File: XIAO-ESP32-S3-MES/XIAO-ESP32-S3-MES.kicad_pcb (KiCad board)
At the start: 2 copper layers, 36 x 39 mm, 11 parts, among them SW1 Conn_01x02_Socket, U2 XIAO-ESP32-S3-SMD

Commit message: SS 配置途中
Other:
- board text added: "5V G A B"
- board text added: "D P G 5V"
- board text added: "L H G 5V"
- board text added: "XIAO ESP32-S3 MES v1.0"
- board text removed: "5V0 G A B"
- board text removed: "D P G 5V0"
- board text removed: "L H G 5V0"
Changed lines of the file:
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@@
 		)
 		(fp_text user "${REFERENCE}"
-			(at 3.75 2.7 90)
-			(layer "F.Fab")
+			(at 3.75 2.7 -90)
+			(layer "B.SilkS")
 			(effects
 				(font
@@
 					(thickness 0.15)
 				)
+				(justify mirror)
 			)
 		)
@@
 		)
 		(fp_text user "${REFERENCE}"
-			(at 1.25 2.7 0)
-			(layer "F.Fab")
+			(at 1.25 2.7 -0)
+			(layer "B.SilkS")
 			(effects
 				(font
@@
 					(thickness 0.15)
 				)
+				(justify mirror)
 			)
 		)
@@
 		)
 		(fp_text user "${REFERENCE}"
-			(at 3.75 2.7 0)
-			(layer "F.Fab")
+			(at 3.75 2.7 -0)
+			(layer "B.SilkS")
 			(effects
 				(font
@@
 					(thickness 0.15)
 				)
+				(justify mirror)
 			)
 		)
@@
 		)
 		(fp_text user "${REFERENCE}"
-			(at 3.75 2.7 90)
-			(layer "F.Fab")
+			(at 3.75 2.7 -90)
+			(layer "B.SilkS")
 			(effects
 				(font
@@
 					(thickness 0.15)
 				)
+				(justify mirror)
 			)
 		)
@@
 		)
 		(fp_text user "${REFERENCE}"
-			(at 3.75 2.7 0)
-			(layer "F.Fab")
+			(at 3.75 2.7 -0)
+			(layer "B.SilkS")
 			(effects
 				(font
@@
 					(thickness 0.15)
 				)
+				(justify mirror)
 			)
 		)
@@
 		)
 		(fp_text user "${REFERENCE}"
-			(at 3.75 2.7 90)
-			(layer "F.Fab")
+			(at 3.75 2.7 -90)
+			(layer "B.SilkS")
 			(effects
 				(font
@@
 					(thickness 0.15)
 				)
+				(justify mirror)
 			)
 		)
@@
 		)
 		(fp_text user "${REFERENCE}"
-			(at 3.75 2.7 90)
-			(layer "F.Fab")
+			(at 3.75 2.7 -90)
+			(layer "B.SilkS")
 			(effects
 				(font
@@
 					(thickness 0.15)
 				)
+				(justify mirror)
 			)
 		)
@@
 		)
 	)
-	(gr_text "D P G 5V0"
+	(gr_text "D P G 5V"
 		(at 98.0948 84.4804 0)
 		(layer "F.SilkS" knockout)
@@
 		)
 	)
-	(gr_text "D P G 5V0"
+	(gr_text "D P G 5V"
 		(at 111.8338 84.5198 0)
 		(layer "F.SilkS" knockout)
@@
 		)
 	)
-	(gr_text "5V0 G A B"
+	(gr_text "5V G A B"
 		(at 104.775 61.007 90)
 		(layer "F.SilkS" knockout)
@@
 		)
 	)
-	(gr_text "5V0 G A B"
+	(gr_text "5V G A B"
 		(at 104.775 74.8792 90)
 		(layer "F.SilkS" knockout)
@@
 		)
 	)
-	(gr_text "L H G 5V0"
+	(gr_text "L H G 5V"
 		(at 126.492 74.7776 90)
 		(layer "F.SilkS" knockout)
@@
 		)
 	)
-	(gr_text "L H G 5V0"
+	(gr_text "L H G 5V"
 		(at 126.515 60.9092 90)
 		(layer "F.SilkS" knockout)
@@
 		)
 	)
+	(gr_text "XIAO ESP32-S3\nMES v1.0"
+		(at 125 79.5 0)
+		(layer "B.SilkS" knockout)
+		(effects
+			(font
+				(size 1 1)
+				(thickness 0.2)
+				(bold yes)
+				(italic yes)
+			)
+			(justify left bottom mirror)
+		)
+	)

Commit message: MES配置完了
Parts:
- added SW2: SW2, Connector_JST:JST_XH_B2B-XH-A_1x02_P2.50mm_Vertical, F.Cu at (128.8, 92.0)
- added SW3: SW3, Connector_JST:JST_XH_B2B-XH-A_1x02_P2.50mm_Vertical, F.Cu at (128.9, 81.9)
- SW1: value Conn_01x02_Socket -> SW1
- moved MD1 11.8 mm to (96.0, 90.3), turned to 90 degrees
- moved R1 11.0 mm to (109.5, 74.8), turned to -90 degrees
- moved MD2 10.6 mm to (111.4, 92.0)
- moved SW1 10.5 mm to (120.1, 92.0)
- moved U1 9.92 mm to (113.0, 76.2), turned to 0 degrees
- moved TERM 6.66 mm to (105.0, 80.5), turned to 180 degrees
- moved ENC1 3.96 mm to (96.0, 62.5)
- moved ENC2 3.96 mm to (96.0, 76.3)
- moved U2 2.23 mm to (103.8, 73.1)
- moved CAN2 1.18 mm to (128.9, 68.5)
- moved CAN1 1.14 mm to (128.9, 55.1)
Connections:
- net ENC2_A renamed ENC2_A/SW2
- net ENC2_B renamed ENC2_B/SW3
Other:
- board size 36 x 39 mm -> 39 x 43 mm
- board text added: "5V G P D"
- board text added: "XIAO ESP32-S3 NHK2027 MES v1.0"
- board text removed: "XIAO ESP32-S3 MES v1.0"

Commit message: MES配線前
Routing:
- added copper zone on B.Cu, net GND
- added copper zone on F.Cu, net GND
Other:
- board text added: "RRST NHK2027 XIAO ESP32-S3 MES v1.0"
- board text removed: "XIAO ESP32-S3 NHK2027 MES v1.0"
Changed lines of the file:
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@@
 		)
 		(fp_text user "${REFERENCE}"
-			(at 1.25 2.7 -0)
+			(at 1.25 2.7 0)
 			(layer "B.SilkS")
 			(effects
@@
 		)
 	)
-	(gr_text "XIAO ESP32-S3\nNHK2027 MES v1.0"
-		(at 118.364 73.152 90)
+	(gr_text "RRST NHK2027\nXIAO ESP32-S3\nMES v1.0"
+		(at 119 74 90)
 		(layer "B.SilkS" knockout)
 		(effects
@@
 		)
 	)
+	(zone
+		(net "GND")
+		(layers "F.Cu" "B.Cu")
+		(hatch edge 0.5)
+		(connect_pads
+			(clearance 0.5)
+		)
+		(min_thickness 0.25)
+		(fill yes
+			(thermal_gap 0.5)
+			(thermal_bridge_width 0.5)
+			(island_removal_mode 0)
+		)
+		(polygon
+			(pts
+				(xy 93 52) (xy 132 52) (xy 132 95) (xy 93 95)
+			)
+		)
+	)

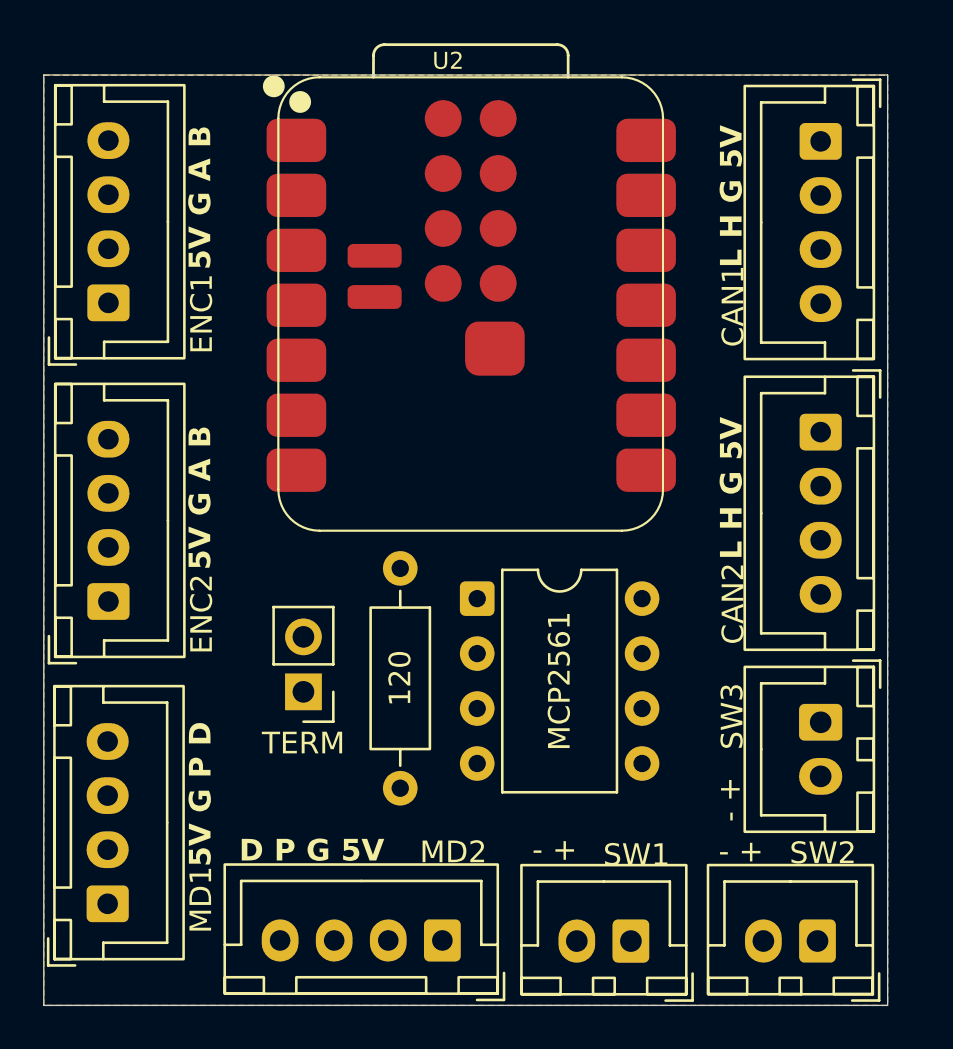
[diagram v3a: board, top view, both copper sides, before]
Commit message: MES自動配線後SS前
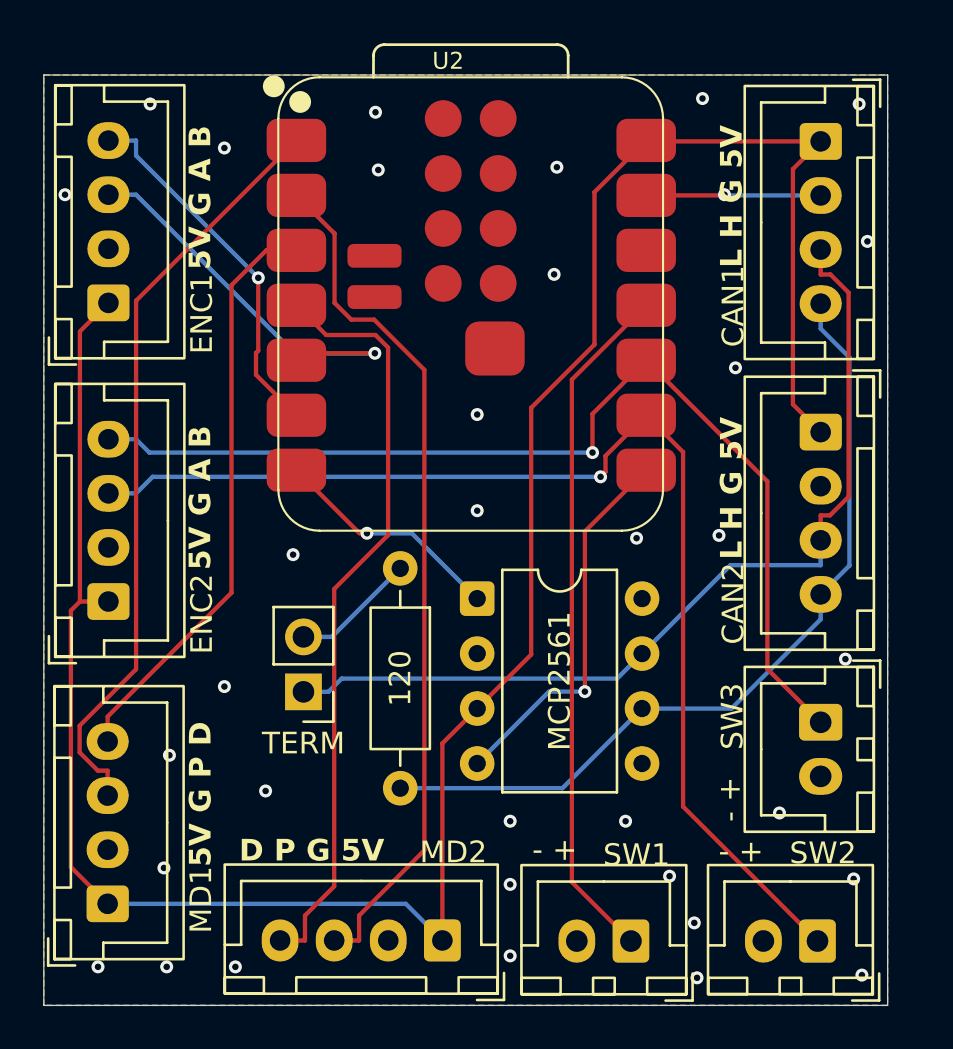
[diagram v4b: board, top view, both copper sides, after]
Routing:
- net 5V0: track 0.00 -> 110.1 mm
- net ENC2_A/SW2: track 0.00 -> 54.4 mm, vias 0 -> 1
- net ENC2_B/SW3: track 0.00 -> 48.0 mm, vias 0 -> 1
- net CANH: track 0.00 -> 42.5 mm
- net GPIO2: track 0.00 -> 39.9 mm
- net CANL: track 0.00 -> 38.4 mm
- net GPIO1: track 0.00 -> 35.2 mm
- net GPIO4: track 0.00 -> 35.2 mm
- net GPIO9: track 0.00 -> 31.9 mm
- net GPIO3: track 0.00 -> 27.1 mm
- net ENC1_A: track 0.00 -> 19.1 mm, vias 0 -> 1
- net CAN_RX: track 0.00 -> 17.8 mm, vias 0 -> 1
- net ENC1_B: track 0.00 -> 17.1 mm, vias 0 -> 1
- net CAN_TX: track 0.00 -> 10.8 mm, vias 0 -> 1
- net GND: track 0.00 -> 8.09 mm, vias 0 -> 35
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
